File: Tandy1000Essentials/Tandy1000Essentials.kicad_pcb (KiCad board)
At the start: 2 copper layers, 99.9 x 99.9 mm, 21 parts, among them J1 IDE_CONNECTOR, J2 CF Adapter Power, J3 Jumpers, J4 Bus_ISA_8bit, U1 BIOS FLASH, U2 74HCT245, U3 GAL22V10, U4 DS1315, U5 AS6C4008-55PCN, Y1 32.768 KHz

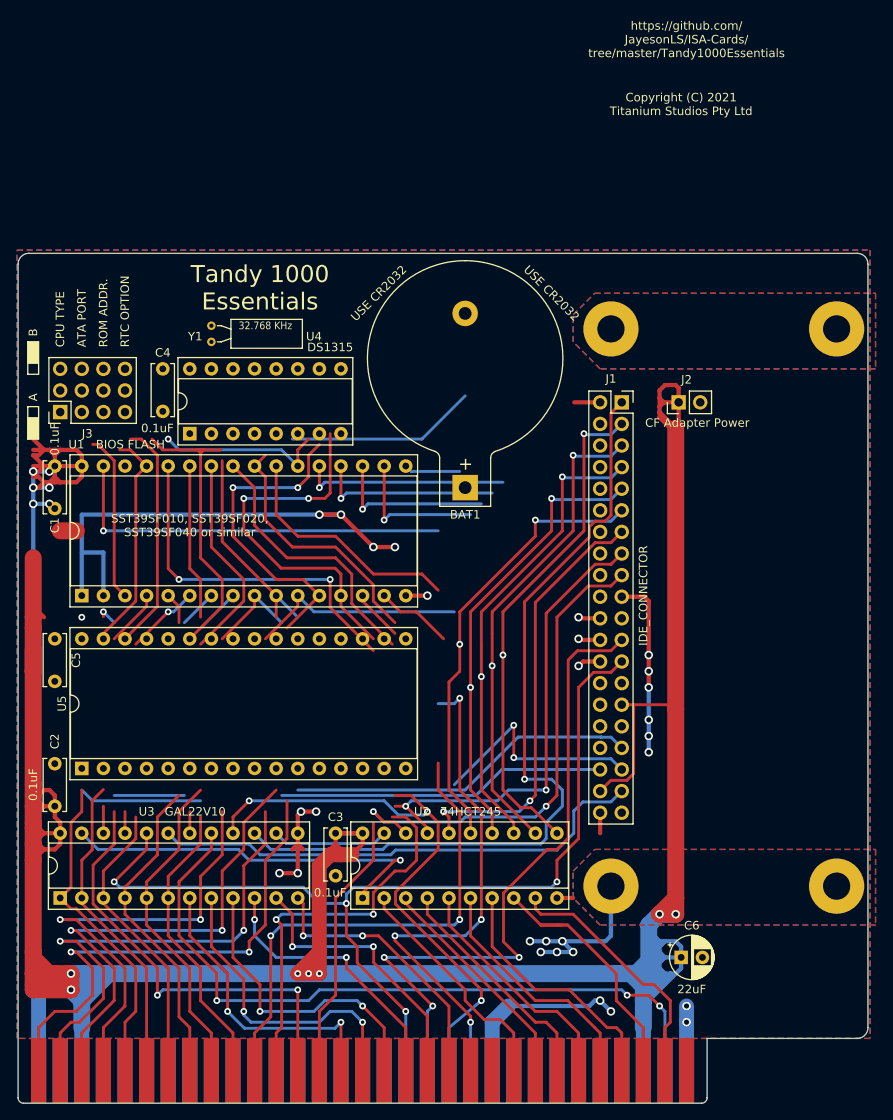
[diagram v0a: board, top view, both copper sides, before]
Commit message: Tandy1000Essentials: Layout passing DRC. Much cleanup still required.
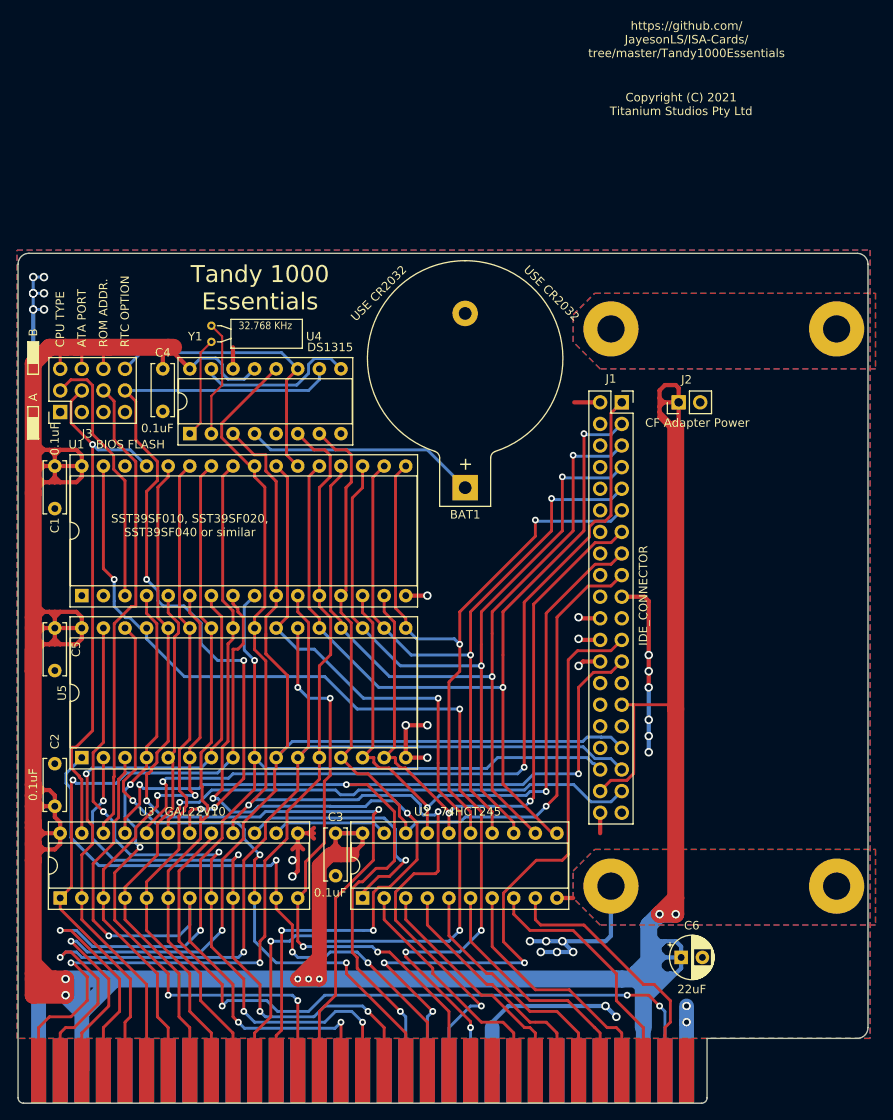
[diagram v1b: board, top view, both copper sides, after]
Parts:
- moved U5 1.27 mm to (104.1, 101.6)
- moved C5 1.27 mm to (101.0, 86.4)
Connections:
- U3 pad 15: ~RESET -> ~IOR_OR_MEMR
- U3 pad 20: ~IOR -> ~RESET
- U3 pad 21: ROM_ADDR_JUMPER -> ~IOR
- U3 pad 22: ATA_ADDR_JUMPER -> ROM_ADDR_JUMPER
- U3 pad 23: ~IOR_OR_MEMR -> ATA_ADDR_JUMPER
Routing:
- net VCC: track 452.8 -> 559.8 mm
- net ~CE~_ROM: track 2.54 -> 90.8 mm, vias 0 -> 4
- net ROM_ADDR_JUMPER: track 3.17 -> 55.8 mm
- net A15: track 36.4 -> 81.6 mm, vias 2 -> 4
- net A18: track 33.3 -> 73.3 mm, vias 2 -> 3
- net A19: track 32.9 -> 69.7 mm, vias 2 -> 4
- net A14: track 35.3 -> 71.8 mm, vias 2 -> 3
- net ATA_ADDR_JUMPER: track 29.2 -> 63.5 mm, vias 0 -> 1
- net A16: track 36.2 -> 70.0 mm, vias 2 -> 4
- net A11: track 78.5 -> 110.5 mm, vias 2 -> 4
- net A13: track 73.8 -> 103.6 mm
- net GND: track 236.8 -> 209.2 mm, vias 34 -> 32
- net ~MEMR: track 100.1 -> 127.3 mm
- net A06: track 43.3 -> 67.4 mm, vias 1 -> 2
- net A02: track 123.3 -> 146.7 mm
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
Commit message: Tandy1000Essentials: More refinement of layout, fix ERC error due to incorrect 22V10 pinout.
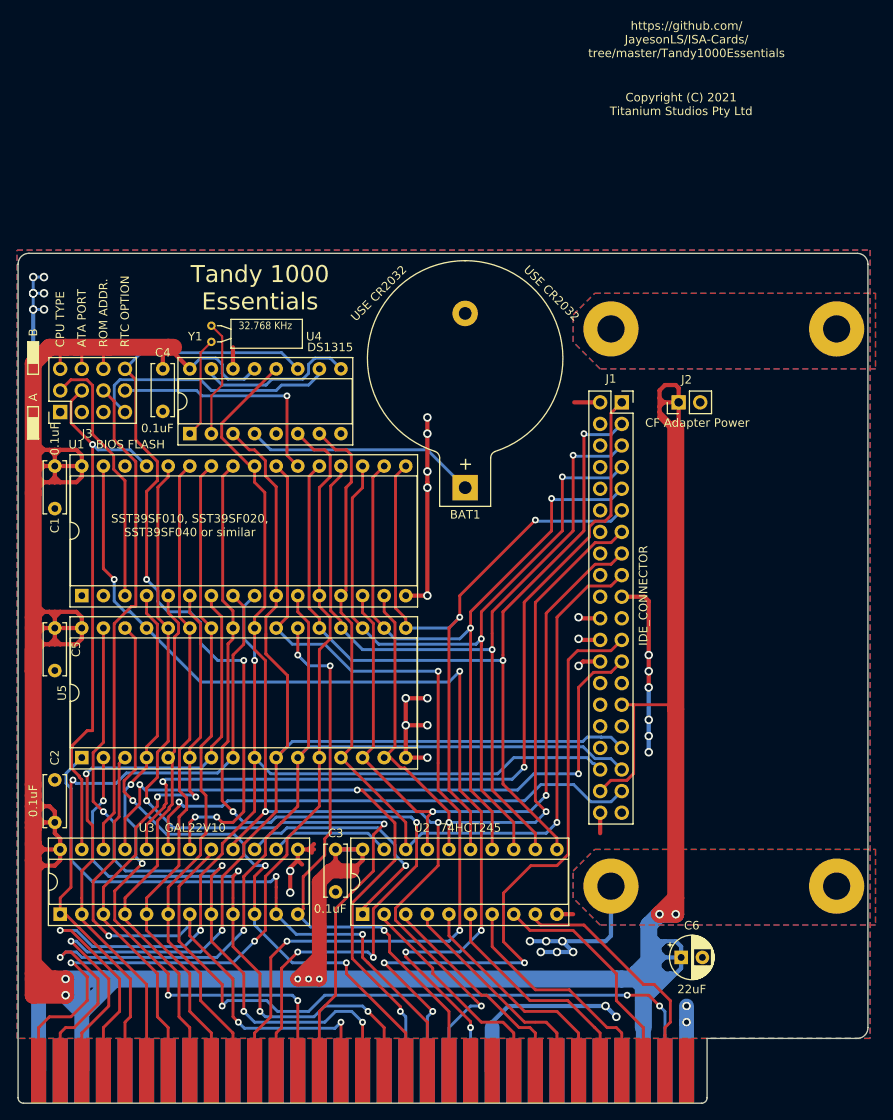
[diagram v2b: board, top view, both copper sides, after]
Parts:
- moved C2 1.91 mm to (101.0, 109.2)
- moved C3 1.91 mm to (134.0, 112.4)
- moved U2 1.91 mm to (137.2, 120.0)
- moved U3 1.91 mm to (101.6, 120.0)
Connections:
- J3 pad 10: Net-(J3-Pad10) -> ~CE~_BIOS_THRU
- J3 pad 11: ~CE~_ROM -> ~CE~_BIOS
- J3 pad 12: ~CE~_BIOS -> ~CE~_BIOS_DECODE
- U3 pad 18: ~CE~_ROM -> ~CE~_BIOS_DECODE
- U4 pad 10: ~CE~_ROM -> ~CE~_BIOS_THRU
- U4 pad 11: ~CE~_BIOS -> ~CE~_BIOS_DECODE
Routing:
- net ~CE~_BIOS_DECODE: track 0.00 -> 94.7 mm, vias 0 -> 4
- net ~CE~_ROM: track 90.8 -> 0.00 mm, vias 4 -> 0
- net ~CE~_BIOS_THRU: track 0.00 -> 30.0 mm
- net GND: track 209.2 -> 233.9 mm, vias 32 -> 38
- net ~CE~_BIOS: track 34.4 -> 28.1 mm, vias 0 -> 1
- net D2_BUF: track 80.5 -> 85.4 mm
- net ~MEMR: track 127.3 -> 122.8 mm
- net ~IOR: track 121.7 -> 117.4 mm
- net A14: track 71.8 -> 68.0 mm
- net D0_BUF: track 105.6 -> 109.4 mm
- net A11: track 110.5 -> 107.5 mm
- net ~MEMW: track 117.6 -> 120.1 mm
- net VCC: track 559.8 -> 557.2 mm
- net D5_BUF: track 90.9 -> 93.2 mm
- net D1_BUF: track 81.1 -> 83.0 mm
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
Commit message: Tandy 1000 Essentials: Finish pass at tidying layout.
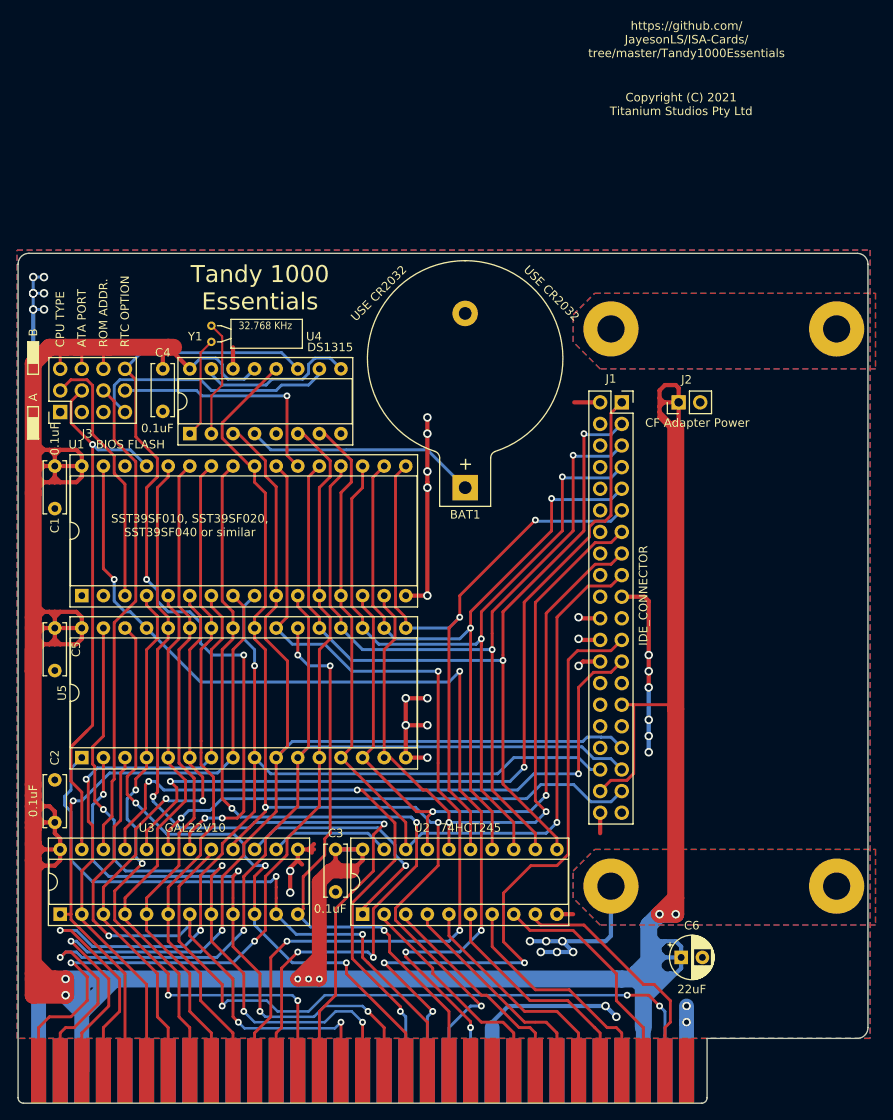
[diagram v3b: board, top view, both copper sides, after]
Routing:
- net ATA_ADDR_JUMPER: track 64.9 -> 67.2 mm
- net A04: track 78.8 -> 76.8 mm
- net ~CS1~_ATA: track 60.8 -> 59.1 mm
- net A07: track 62.5 -> 63.9 mm
- net A13: track 103.2 -> 102.2 mm
- net ~CE~_BIOS_DECODE: track 94.7 -> 93.8 mm
- net A08: track 78.1 -> 78.9 mm
- net A09: track 77.8 -> 78.6 mm
- net A06: track 67.7 -> 68.4 mm
- net A11: track 107.5 -> 106.9 mm

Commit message: Change .34/.35mm tracks to .3mm.
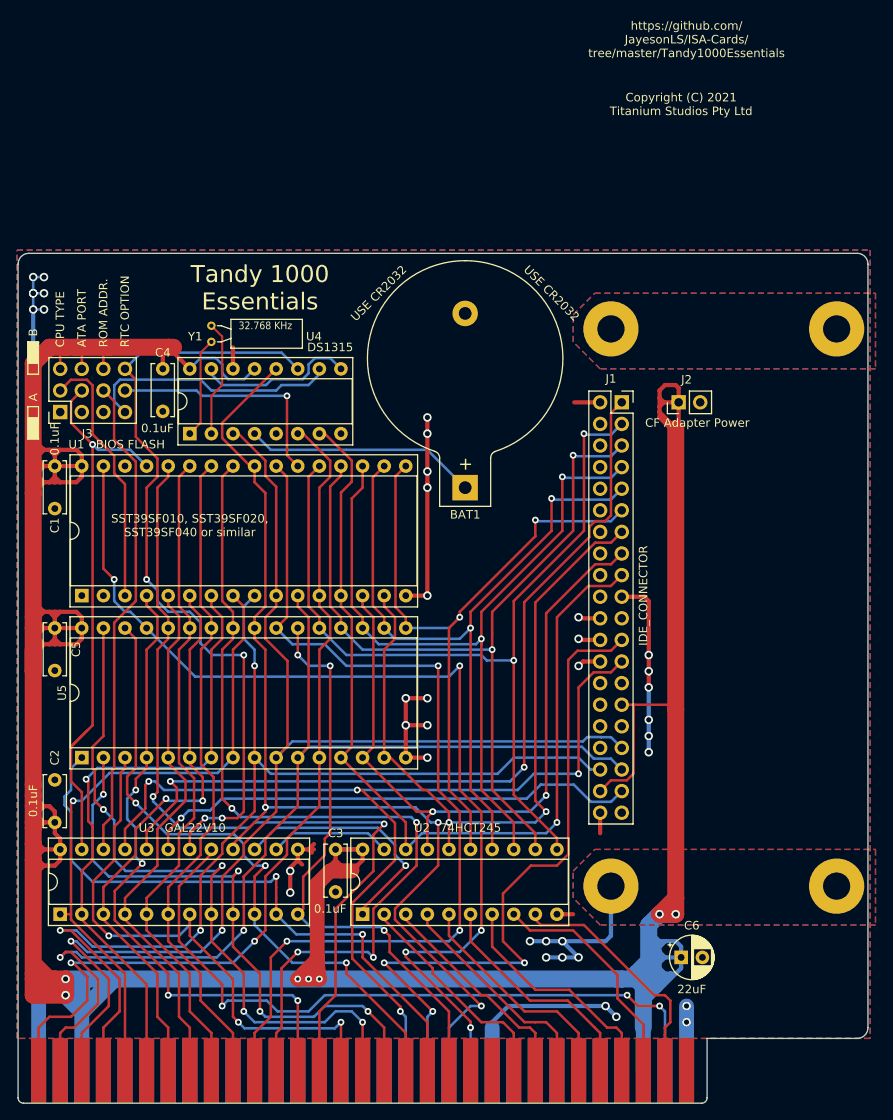
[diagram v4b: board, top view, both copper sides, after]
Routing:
- net VCC: track 557.2 -> 559.4 mm
- net GND: track 233.9 -> 234.8 mm
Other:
- net class Crystal: clearance 0.24 -> 0.26
- net class Default: clearance 0.24 -> 0.26; trace_width 0.34 -> 0.3
- net class Power: clearance 0.24 -> 0.26
- rule trace_clearance: 0.24 -> 0.26

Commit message: Fix location of CF adapter power for all boards that use it. Also the mounting holes in the schematic for the same boards. Finishing touches to Tandy 1000 Essentials.
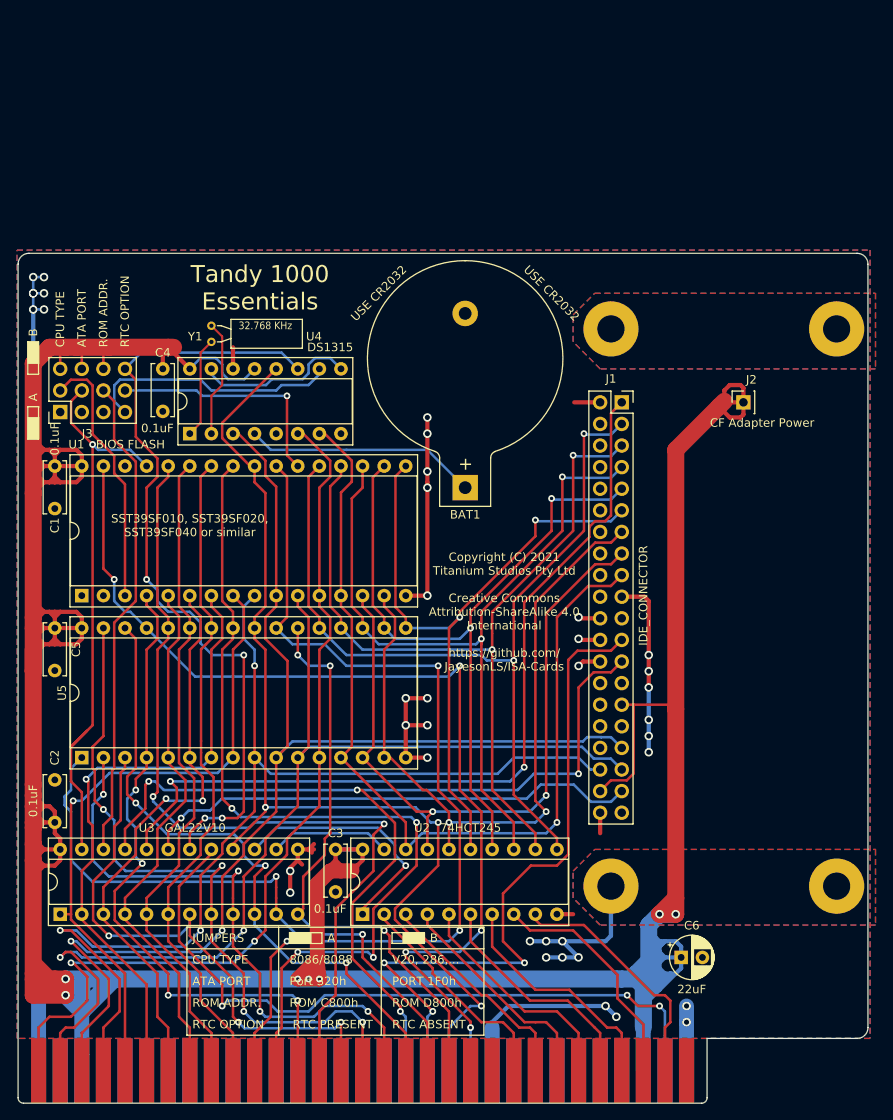
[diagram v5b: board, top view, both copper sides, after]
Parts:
- H1: renamed from MH1; value MH -> MountingHole_Pad
- H2: renamed from MH2; value MH -> MountingHole_Pad
- H3: renamed from MH3; value MH -> MountingHole_Pad
- H4: renamed from MH4; value MH -> MountingHole_Pad
- J2: footprint Connector_PinHeader_2.54mm:PinHeader_1x02_P2.54mm_Vertical -> Connector_PinSocket_2.54mm:PinSocket_1x01_P2.54mm_Vertical
- moved J2 7.62 mm to (182.0, 59.8)
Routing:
- net VCC: track 559.4 -> 560.1 mm
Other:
- board text added: "8086/8088"
- board text added: "Copyright (C) 2021 Titanium Studios Pty Ltd Creative Commons Attribution-ShareAlike 4.0 International https://github.com/ JayesonLS/ISA-Cards"
- board text added: "JUMPERS"
- board text added: "PORT 1F0h"
- board text added: "Port 320h"
- board text added: "ROM C800h"
- board text added: "ROM D800h"
- board text added: "RTC ABSENT"
- board text added: "RTC PRESENT"
- board text added: "V20, 286,..."
- board text removed: "Copyright (C) 2021 Titanium Studios Pty Ltd"
- board text removed: "https://github.com/ JayesonLS/ISA-Cards/ tree/master/Tandy1000Essentials"
